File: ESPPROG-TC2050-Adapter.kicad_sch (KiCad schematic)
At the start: 6 parts, among them J1 DebugHeader_Cortex-M_JTAG_10p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, J2 CONN ESP-PROG, J3 2x3 Card Edge Progamming Conn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, U1 GT-USB-7010ASV

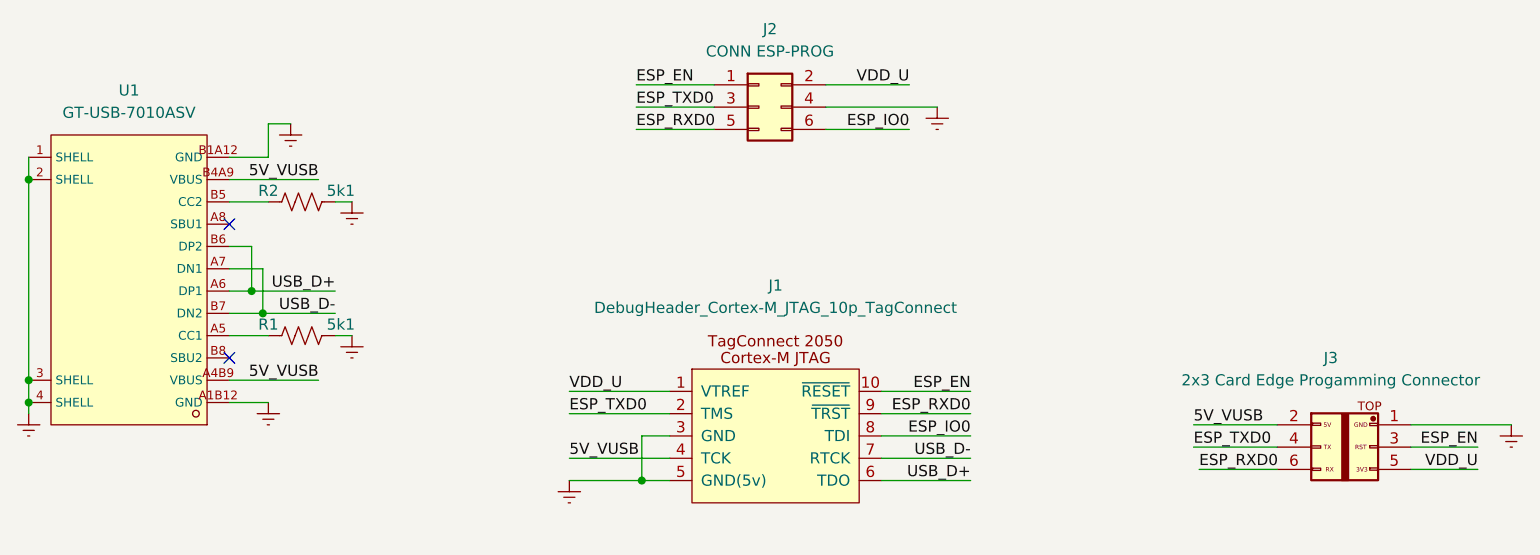
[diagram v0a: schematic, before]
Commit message: Majority of v1.1 changes
* Removed card-edge connector
* Added SOICbite 2x4P 2.54mm header with ESP8266 pinout
* changed TC-2050 pinout to more default UART one
* changed board dimensions to better fit on top of ESP-PROG
* added to-scale picture of ESP-PROG in background to get better feel
  for alignment
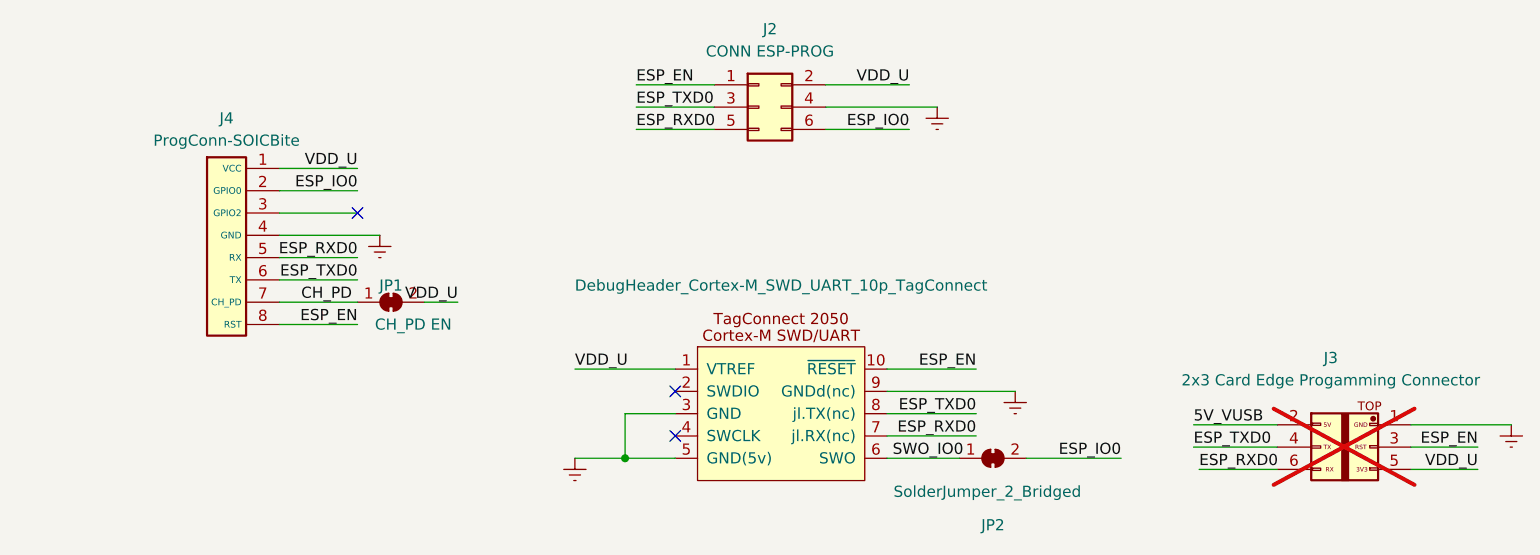
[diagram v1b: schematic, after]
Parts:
- removed J1: DebugHeader_Cortex-M_JTAG_10p_TagConnect, Connector_PinSocket_1.27mm:PinSocket_2x05_P1.27mm_Vertical, symbol BrechtVE_DebugHeader:DebugHeader_Cortex-M_JTAG_10p_TagConnect
- removed R1, R2: 5k1, Resistor_SMD:R_0805_2012Metric_Pad1.20x1.40mm_HandSolder, symbol Device:R_US
- removed U1: GT-USB-7010ASV, jmux-footprints:USB-C-SMD_G-SWITCH_GT-USB-7010ASV, symbol gt-usb_lib:GT-USB-7010ASV
- added J4: ProgConn-SOICBite, Connector_IDC:IDC-Header_2x04_P2.54mm_Vertical, symbol jmux-kicadlib:SOICbite-ESP8266
- added J5: DebugHeader_Cortex-M_SWD_UART_10p_TagConnect, jmux-footprints:TC-2050-IDC-SOCKET, symbol BrechtVE_DebugHeader:DebugHeader_Cortex-M_SWD_UART_10p_TagConnect
- added JP1: CH_PD EN, Jumper:SolderJumper-2_P1.3mm_Bridged_RoundedPad1.0x1.5mm, symbol Jumper:SolderJumper_2_Bridged
- added JP2: SolderJumper_2_Bridged, Jumper:SolderJumper-2_P1.3mm_Bridged_RoundedPad1.0x1.5mm, symbol Jumper:SolderJumper_2_Bridged
- J3: now not fitted
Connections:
- net ESP_EN: now also J4.8 (RST), J5.10 (~{RESET})
- net ESP_IO0: now also J4.2 (GPIO0), JP2.2 (B)
- net ESP_RXD0: now also J4.5 (RX), J5.7 (jl.RX(nc))
- net ESP_TXD0: now also J4.6 (TX), J5.8 (jl.TX(nc))
- net Earth: now also J4.4 (GND), J5.3 (GND), J5.5 (GND(5v)), J5.9 (GNDd(nc))
- net VDD_U: now also J4.1 (VCC), J5.1 (VTREF), JP1.2 (B)
- new net CH_PD: J4.7 (CH_PD), JP1.1 (A)
- new net SWO_IO0: J5.6 (SWO), JP2.1 (A)
- no-connect marks 2 -> 3
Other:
- company: (none) -> jacobbokor.com
- title: ESP-PROG to TC-2050 and Card Edge Connector -> ESP-PROG Board Connector Adapter

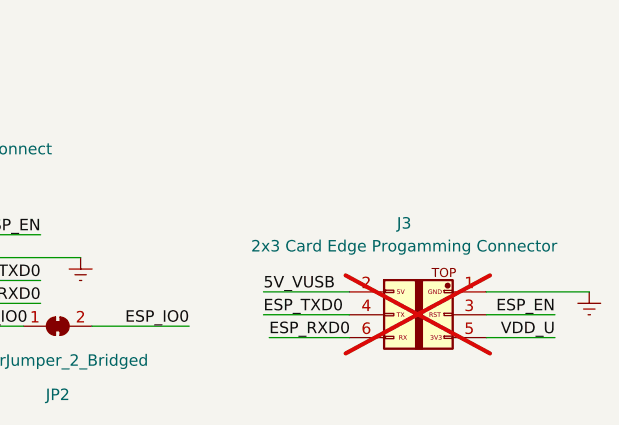
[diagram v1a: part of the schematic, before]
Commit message: updated BOM fields and added LCSC PNs
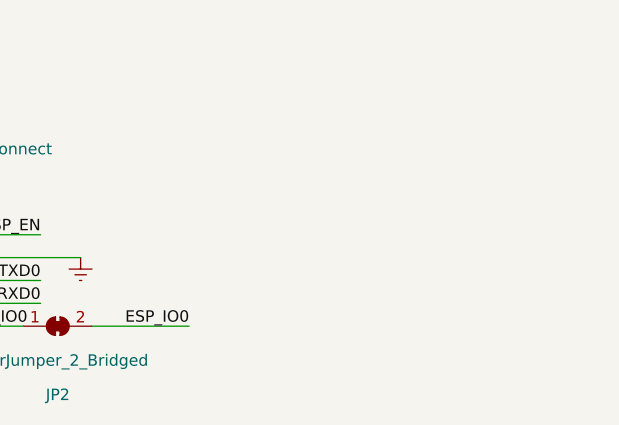
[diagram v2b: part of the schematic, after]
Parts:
- removed J3: 2x3 Card Edge Progamming Connector, Connector_PinHeader_2.54mm:PinHeader_2x03_P2.54mm_Vertical, symbol jmux-kicadlib:2x3_Card_Edge_UART_Connector
- J2: LCSC (none) -> C5298392; Link (none) -> https://www.lcsc.com/product-detail/span-style-background-c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
- J4: LCSC (none) -> C17179451; Link (none) -> https://www.lcsc.com/product-detail/IDC-Connectors_HanElect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
- J5: LCSC (none) -> C2962228; Link (none) -> https://www.lcsc.com/product-detail/_XKB-Connectivity-_C296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
- JP1, JP2: now left out of the parts list
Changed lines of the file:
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@@
   (no_connect (at 116.205 60.325))
   (no_connect (at 152.4 80.645))
-  (wire (pts (xy 211.455 86.995) (xy 220.98 86.995))
-    (stroke (width 0) (type default))
-  )
   (wire (pts (xy 123.825 70.485) (xy 127.635 70.485))
     (stroke (width 0) (type default))
@@
     (stroke (width 0) (type default))
   )
-  (wire (pts (xy 212.09 89.535) (xy 220.98 89.535))
-    (stroke (width 0) (type default))
-  )
   (wire (pts (xy 107.315 70.485) (xy 116.205 70.485))
     (stroke (width 0) (type default))
@@
     (stroke (width 0) (type default))
   )
-  (wire (pts (xy 211.455 84.455) (xy 220.98 84.455))
-    (stroke (width 0) (type default))
-  )
   (wire (pts (xy 107.315 57.785) (xy 116.205 57.785))
     (stroke (width 0) (type default))
   )
-  (wire (pts (xy 236.22 89.535) (xy 243.84 89.535))
-    (stroke (width 0) (type default))
-  )
   (wire (pts (xy 192.405 88.265) (xy 203.2 88.265))
     (stroke (width 0) (type default))
   )
-  (wire (pts (xy 236.22 84.455) (xy 247.65 84.455))
-    (stroke (width 0) (type default))
-  )
   (wire (pts (xy 107.315 67.945) (xy 116.205 67.945))
     (stroke (width 0) (type default))
@@
     (stroke (width 0) (type default))
   )
-  (wire (pts (xy 236.22 86.995) (xy 243.84 86.995))
-    (stroke (width 0) (type default))
-  )
-  (label "ESP_RXD0" (at 212.09 89.535 0) (fields_autoplaced)
-    (effects (font (size 1.27 1.27)) (justify left bottom))
-  )
-  (label "ESP_EN" (at 243.84 86.995 180) (fields_autoplaced)
-    (effects (font (size 1.27 1.27)) (justify right bottom))
-  )
   (label "ESP_EN" (at 147.955 45.72 0) (fields_autoplaced)
     (effects (font (size 1.27 1.27)) (justify left bottom))
@@
     (effects (font (size 1.27 1.27)) (justify right bottom))
   )
-  (label "5V_VUSB" (at 211.455 84.455 0) (fields_autoplaced)
-    (effects (font (size 1.27 1.27)) (justify left bottom))
-  )
   (label "ESP_RXD0" (at 186.69 85.725 180) (fields_autoplaced)
     (effects (font (size 1.27 1.27)) (justify right bottom))
   )
-  (label "ESP_TXD0" (at 211.455 86.995 0) (fields_autoplaced)
-    (effects (font (size 1.27 1.27)) (justify left bottom))
-  )
   (label "ESP_IO0" (at 203.2 88.265 180) (fields_autoplaced)
     (effects (font (size 1.27 1.27)) (justify right bottom))
@@
   )
   (label "VDD_U" (at 116.205 55.245 180) (fields_autoplaced)
-    (effects (font (size 1.27 1.27)) (justify right bottom))
-  )
-  (label "VDD_U" (at 243.84 89.535 180) (fields_autoplaced)
     (effects (font (size 1.27 1.27)) (justify right bottom))
   )
@@
     )
     (property "Datasheet" "" (at 109.855 76.835 0)
+      (effects (font (size 1.27 1.27)) hide)
+    )
+    (property "LCSC" "C17179451" (at 109.855 76.835 0)
+      (effects (font (size 1.27 1.27)) hide)
+    )
+    (property "Link" "https://www.lcsc.com/product-detail/IDC-Connectors_HanElectricity-HY2541WV-N-2x4P_C17179451.html" (at 109.855 76.835 0)
+      (effects (font (size 1.27 1.27)) hide)
+    )
+    (property "Description" "2x4P 2.54mm IDC header for SOICbite" (at 109.855 76.835 0)
       (effects (font (size 1.27 1.27)) hide)
     )
@@
     )
   )
-  (symbol (lib_id "power:Earth") (at 247.65 84.455 0) (unit 1)
-    (in_bom yes) (on_board yes) (dnp no) (fields_autoplaced)
-    (property "Reference" "#PWR08" (at 247.65 90.805 0)
-      (effects (font (size 1.27 1.27)) hide)
-    )
-    (property "Value" "Earth" (at 247.65 88.265 0)
-      (effects (font (size 1.27 1.27)) hide)
-    )
-    (property "Footprint" "" (at 247.65 84.455 0)
-      (effects (font (size 1.27 1.27)) hide)
-    )
-    (property "Datasheet" "~" (at 247.65 84.455 0)
-      (effects (font (size 1.27 1.27)) hide)
-    )
-    (pin "1")
-    (instances
-      (project "ESPPROG-TC2050-Adapter"
-        (path "/0deeddec-331d-4e7e-80f3-64b8c983bbee"
-          (reference "#PWR08") (unit 1)
-        )
-      )
-    )
-  )
   (symbol (lib_id "Jumper:SolderJumper_2_Bridged") (at 188.595 88.265 0) (unit 1)
-    (in_bom yes) (on_board yes) (dnp no)
+    (in_bom no) (on_board yes) (dnp no)
     (property "Reference" "JP2" (at 188.595 95.885 0)
       (effects (font (size 1.27 1.27)))
@@
     )
     (property "Datasheet" "~" (at 161.925 48.26 0)
+      (effects (font (size 1.27 1.27)) hide)
+    )
+    (property "Description" "2x3 2.54mm Male IDC header for connecting to ESP-PROG" (at 161.925 48.26 0)
+      (effects (font (size 1.27 1.27)) hide)
+    )
+    (property "LCSC" "C5298392" (at 161.925 48.26 0)
+      (effects (font (size 1.27 1.27)) hide)
+    )
+    (property "Link" "https://www.lcsc.com/product-detail/span-style-background-color-ff0-Female-span-span-style-background-color-ff0-Headers-span_CJT-Changjiang-Connectors-A2541HWV-2x3P_C5298392.html" (at 161.925 48.26 0)
       (effects (font (size 1.27 1.27)) hide)
     )
@@
   )
   (symbol (lib_id "Jumper:SolderJumper_2_Bridged") (at 120.015 70.485 0) (unit 1)
-    (in_bom yes) (on_board yes) (dnp no)
+    (in_bom no) (on_board yes) (dnp no)
     (property "Reference" "JP1" (at 120.015 68.58 0)
       (effects (font (size 1.27 1.27)))
@@
     )
   )
-  (symbol (lib_id "jmux-kicadlib:2x3_Card_Edge_UART_Connector") (at 226.695 83.185 0) (unit 1)
-    (in_bom no) (on_board no) (dnp yes) (fields_autoplaced)
-    (property "Reference" "J3" (at 227.0855 76.835 0)
-      (effects (font (size 1.27 1.27)))
-    )
-    (property "Value" "2x3 Card Edge Progamming Connector" (at 227.0855 79.375 0)
-      (effects (font (size 1.27 1.27)))
-    )
-    (property "Footprint" "Connector_PinHeader_2.54mm:PinHeader_2x03_P2.54mm_Vertical" (at 229.4255 86.5759 0)
-      (effects (font (size 1.27 1.27)) hide)
-    )
-    (property "Datasheet" "~" (at 229.4255 86.5759 0)
-      (effects (font (size 1.27 1.27)) hide)
-    )
-    (property "Sim.Enable" "0" (at 226.695 83.185 0)
-      (effects (font (size 1.27 1.27)) hide)
-    )
-    (pin "1")
-    (pin "2")
-    (pin "3")
-    (pin "4")
-    (pin "5")
-    (pin "6")
-    (instances
-      (project "ESPPROG-TC2050-Adapter"
-        (path "/0deeddec-331d-4e7e-80f3-64b8c983bbee"
-          (reference "J3") (unit 1)
-        )
-      )
-    )
-  )
   (symbol (lib_id "BrechtVE_DebugHeader:DebugHeader_Cortex-M_SWD_UART_10p_TagConnect") (at 163.83 83.185 0) (unit 1)
     (in_bom yes) (on_board yes) (dnp no) (fields_autoplaced)
@@
       (effects (font (size 1.27 1.27)) hide)
     )
+    (property "LCSC" "C2962228" (at 163.83 83.185 0)
+      (effects (font (size 1.27 1.27)) hide)
+    )
+    (property "Link" "https://www.lcsc.com/product-detail/_XKB-Connectivity-_C2962228.html" (at 163.83 83.185 0)
+      (effects (font (size 1.27 1.27)) hide)
+    )
+    (property "Description" "2x5P 1.27mm IDC header for tag-connect TC-2050-IDC cable" (at 163.83 83.185 0)
+      (effects (font (size 1.27 1.27)) hide)
+    )

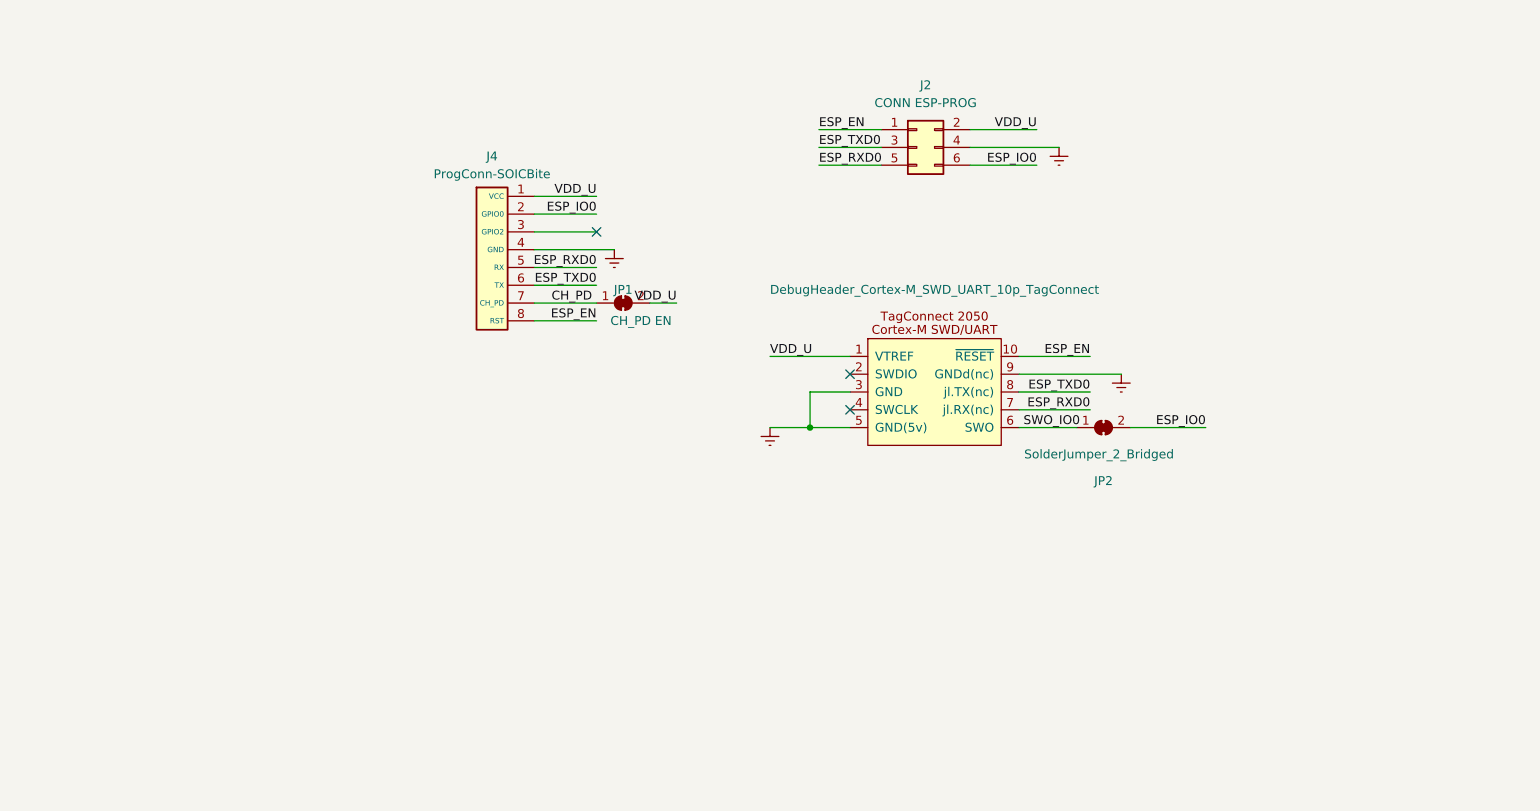
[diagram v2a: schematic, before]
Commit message: Redesign for v1.2
* Added second F header to connect to ESP-PROG's JTAG header
* added connectors for TC2050 and SOICbite for JTAG
* had to extend board length as a result
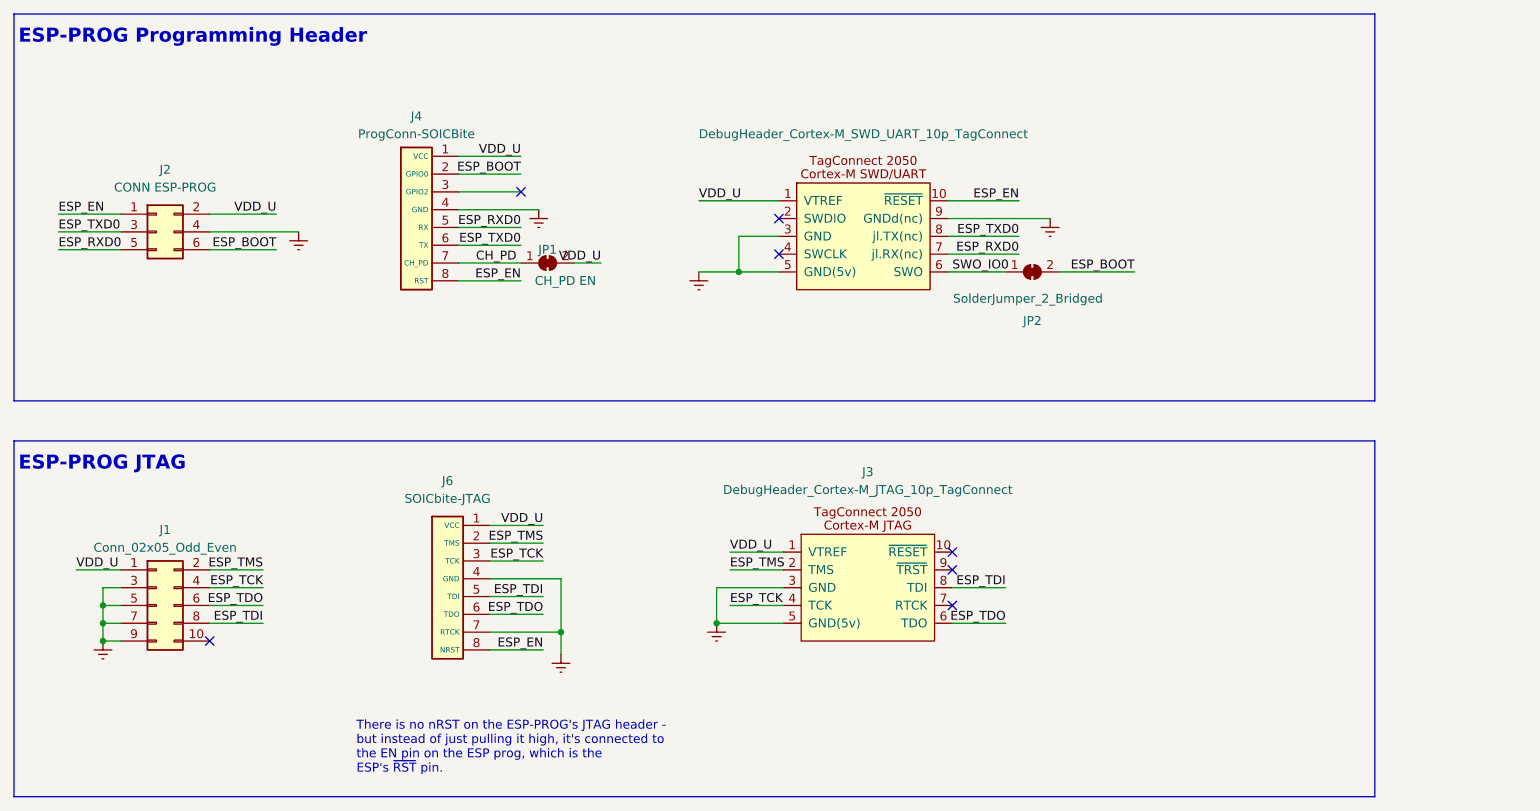
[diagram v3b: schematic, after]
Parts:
- added J1: Conn_02x05_Odd_Even, Connector_PinSocket_2.54mm:PinSocket_2x05_P2.54mm_Vertical, symbol Connector_Generic:Conn_02x05_Odd_Even
- added J3: DebugHeader_Cortex-M_JTAG_10p_TagConnect, jmux-footprints:TC-2050-IDC-SOCKET, symbol BrechtVE_DebugHeader:DebugHeader_Cortex-M_JTAG_10p_TagConnect
- added J6: SOICbite-JTAG, Connector_IDC:IDC-Header_2x04_P2.54mm_Vertical, symbol jmux-kicadlib:SOICbite-JTAG
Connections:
- net ESP_EN: now also J6.8 (NRST)
- net Earth: now also J1.3 (Pin_3), J1.5 (Pin_5), J1.7 (Pin_7), J1.9 (Pin_9), J3.3 (GND), J3.5 (GND(5v)), J6.4 (GND), J6.7 (RTCK)
- net VDD_U: now also J1.1 (Pin_1), J3.1 (VTREF), J6.1 (VCC)
- net ESP_IO0 renamed ESP_BOOT
- new net ESP_TCK: J1.4 (Pin_4), J3.4 (TCK), J6.3 (TCK)
- new net ESP_TDI: J1.8 (Pin_8), J3.8 (TDI), J6.5 (TDI)
- new net ESP_TDO: J1.6 (Pin_6), J3.6 (TDO), J6.6 (TDO)
- new net ESP_TMS: J1.2 (Pin_2), J3.2 (TMS), J6.2 (TMS)
- no-connect marks 3 -> 7
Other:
- note added: "ESP-PROG JTAG"
- note added: "ESP-PROG Programming Header"
- note added: "There is no nRST on the ESP-PROG's JTAG header - but instead of just pulling it high, it's connected to the EN pin on the ESP prog, which is the ESP's ~{RST} pin."
- moved on the sheet: J2, J4, JP1, JP2
